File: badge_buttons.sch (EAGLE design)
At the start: 6 parts

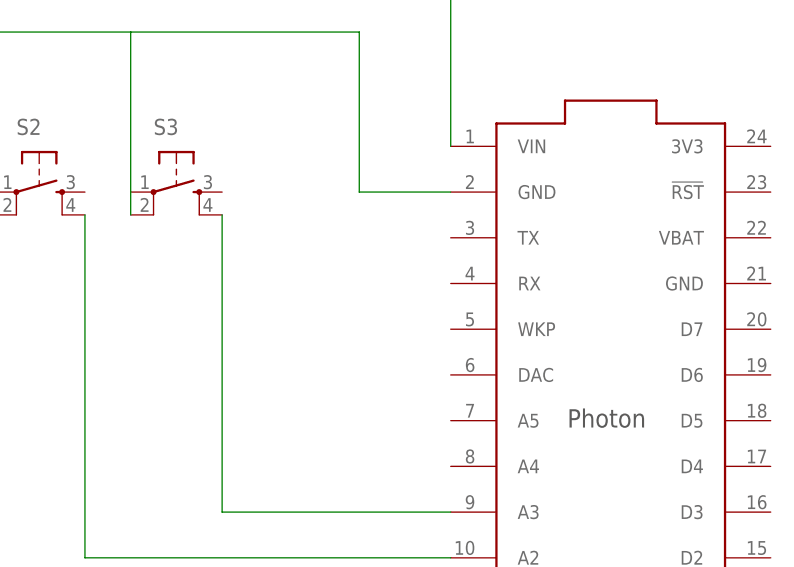
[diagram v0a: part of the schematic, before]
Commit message: clean up lines, add sensor loop
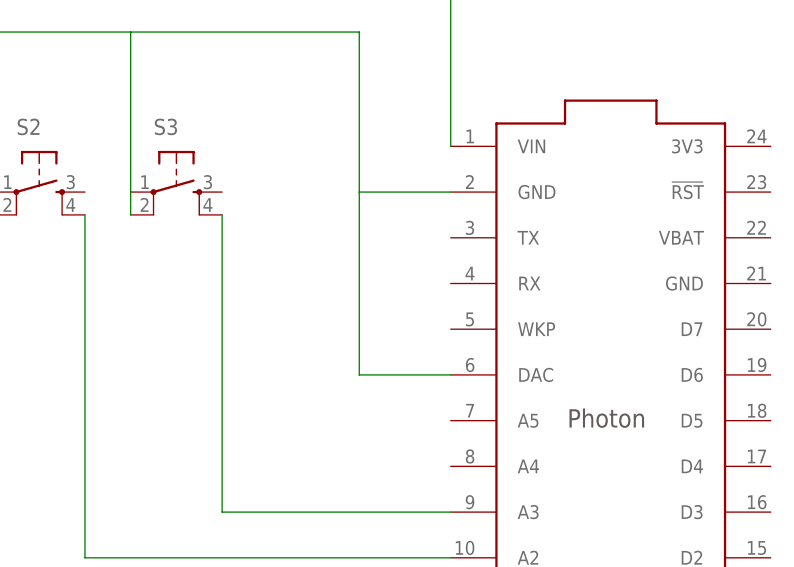
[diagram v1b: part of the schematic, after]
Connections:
- net N$4: now also U$1.DAC
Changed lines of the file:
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@@
 <pinref part="S3" gate="S" pin="2"/>
 <wire x1="43.18" y1="50.8" x2="43.18" y2="48.26" width="0.1524" layer="91"/>
+<pinref part="U$1" gate="G$1" pin="DAC"/>
+<wire x1="78.74" y1="30.48" x2="68.58" y2="30.48" width="0.1524" layer="91"/>
+<wire x1="68.58" y1="30.48" x2="68.58" y2="50.8" width="0.1524" layer="91"/>
 </segment>
 </net>

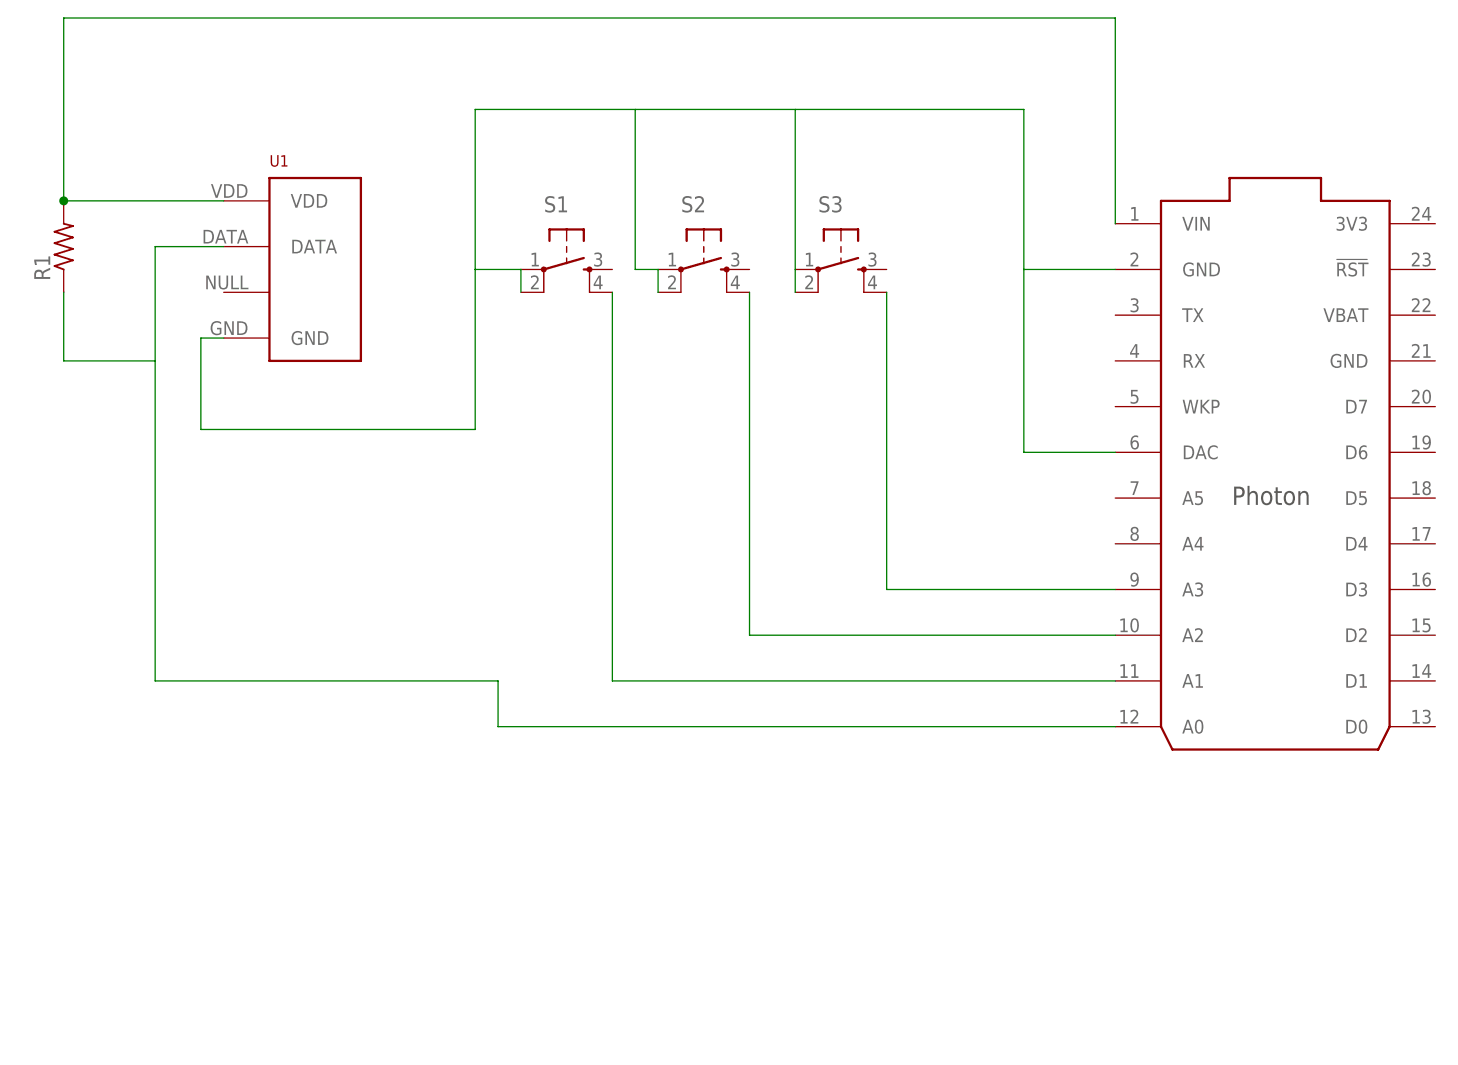
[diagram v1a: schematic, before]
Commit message: MLX succesfully added to code
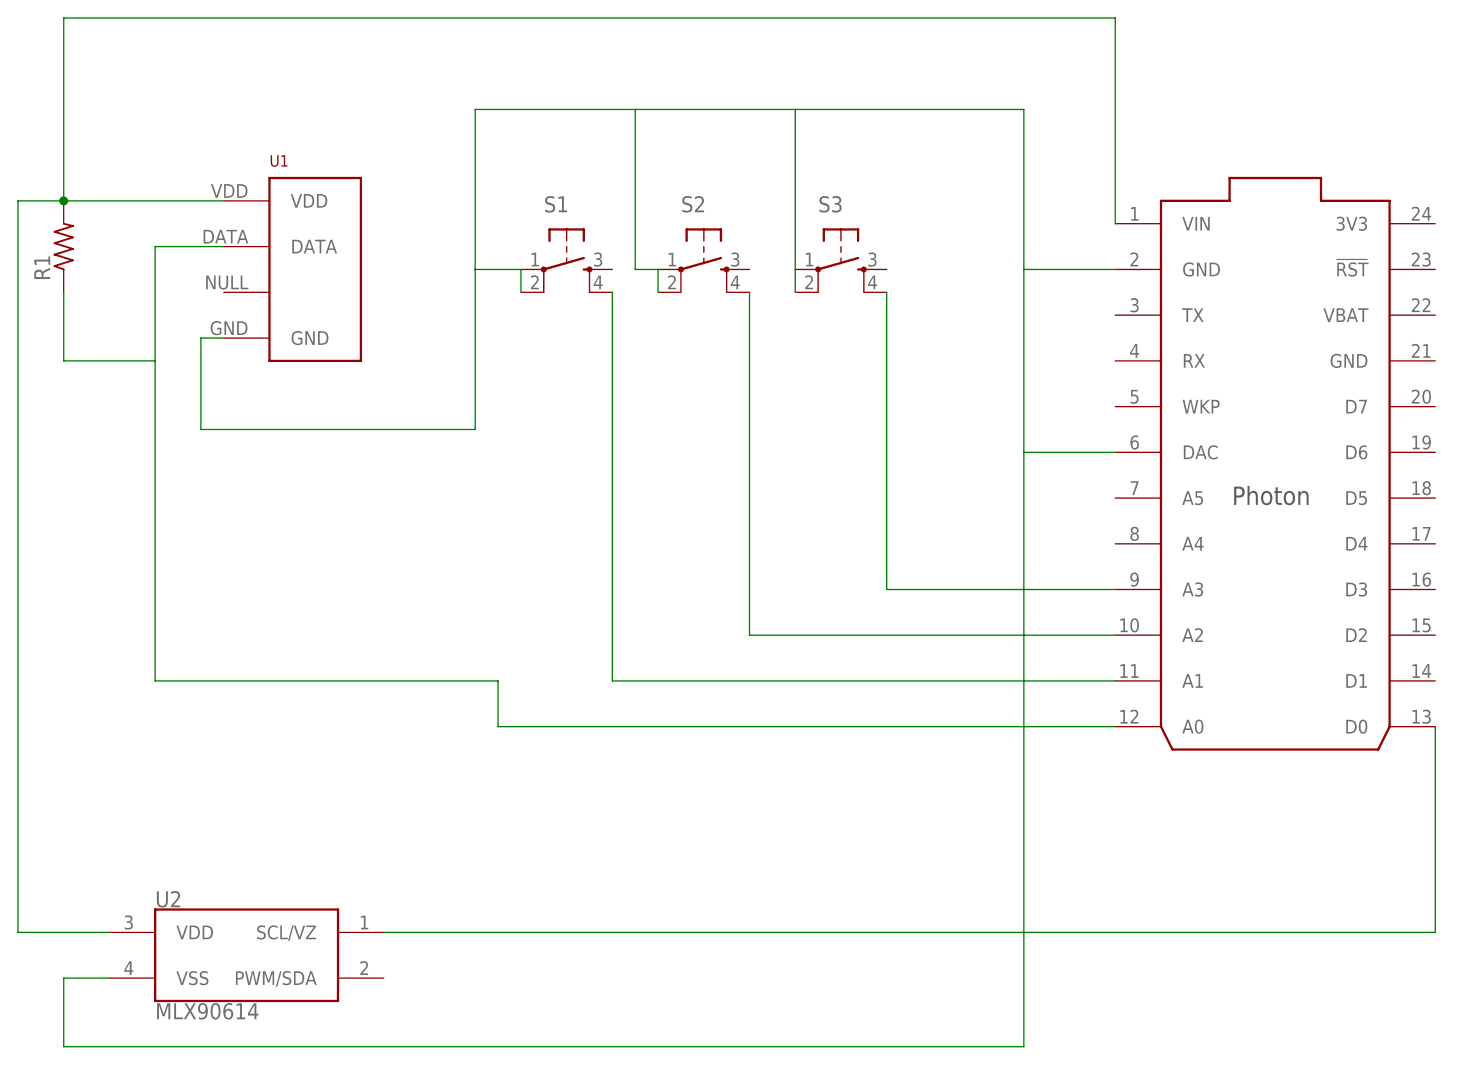
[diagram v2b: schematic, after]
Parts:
- added U2: MLX90614, SparkFun-Sensors:MLX90614
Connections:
- new net N$7: U$1.D0, U2.SCL/VZ
- net N$4: now also U2.VSS
- net N$5: now also U2.VDD
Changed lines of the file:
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@@
 <part name="U1" library="RHT03_DHT-22_AM2302" deviceset="RHT03_DHT-22_AM2302" device=""/>
 <part name="R1" library="resistor" library_urn="urn:adsk.eagle:library:348" deviceset="R-US_" device="0204/7" package3d_urn="urn:adsk.eagle:package:25945/1"/>
+<part name="U2" library="SparkFun-Sensors" deviceset="MLX90614" device=""/>
 </parts>
 <sheets>
@@
 <instance part="U1" gate="G$1" x="-10.16" y="50.8"/>
 <instance part="R1" gate="G$1" x="-38.1" y="53.34" rot="R90"/>
+<instance part="U2" gate="G$1" x="-17.78" y="-25.4"/>
 </instances>
 <busses>
@@
 <wire x1="78.74" y1="30.48" x2="68.58" y2="30.48" width="0.1524" layer="91"/>
 <wire x1="68.58" y1="30.48" x2="68.58" y2="50.8" width="0.1524" layer="91"/>
+<pinref part="U2" gate="G$1" pin="VSS"/>
+<wire x1="-33.02" y1="-27.94" x2="-38.1" y2="-27.94" width="0.1524" layer="91"/>
+<wire x1="-38.1" y1="-27.94" x2="-38.1" y2="-35.56" width="0.1524" layer="91"/>
+<wire x1="-38.1" y1="-35.56" x2="68.58" y2="-35.56" width="0.1524" layer="91"/>
+<wire x1="68.58" y1="-35.56" x2="68.58" y2="30.48" width="0.1524" layer="91"/>
 </segment>
 </net>
@@
 <pinref part="R1" gate="G$1" pin="2"/>
 <junction x="-38.1" y="58.42"/>
+<wire x1="-38.1" y1="58.42" x2="-43.18" y2="58.42" width="0.1524" layer="91"/>
+<pinref part="U2" gate="G$1" pin="VDD"/>
+<wire x1="-43.18" y1="58.42" x2="-43.18" y2="-22.86" width="0.1524" layer="91"/>
+<wire x1="-43.18" y1="-22.86" x2="-33.02" y2="-22.86" width="0.1524" layer="91"/>
 </segment>
 </net>
@@
 </segment>
 </net>
+<net name="N$7" class="0">
+<segment>
+<pinref part="U2" gate="G$1" pin="SCL/VZ"/>
+<pinref part="U$1" gate="G$1" pin="D0"/>
+<wire x1="-2.54" y1="-22.86" x2="114.3" y2="-22.86" width="0.1524" layer="91"/>
+<wire x1="114.3" y1="-22.86" x2="114.3" y2="0" width="0.1524" layer="91"/>
+</segment>
+</net>
